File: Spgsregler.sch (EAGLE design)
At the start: 13 parts, among them X4 22-23-2031, X5 22-23-2031

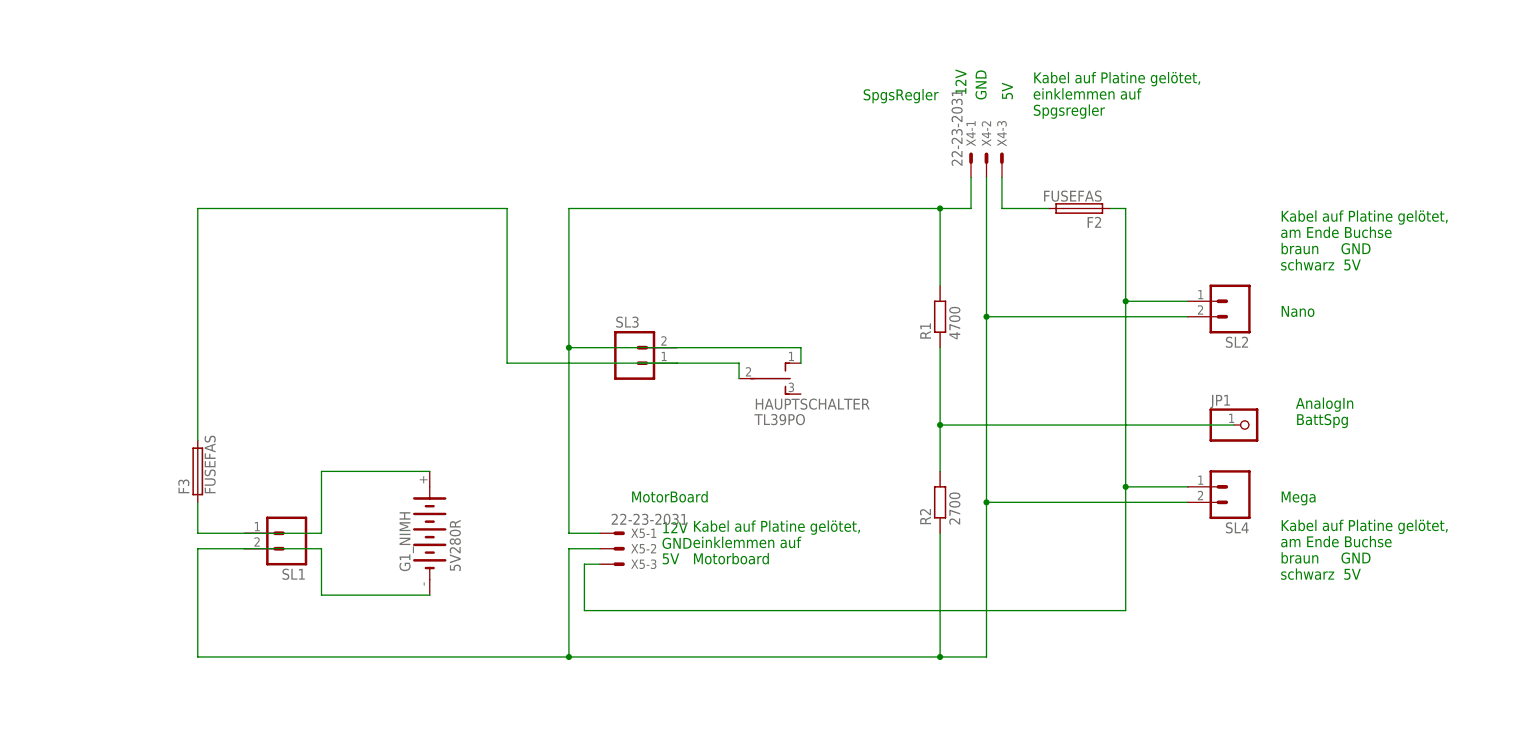
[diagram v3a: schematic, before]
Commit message: 
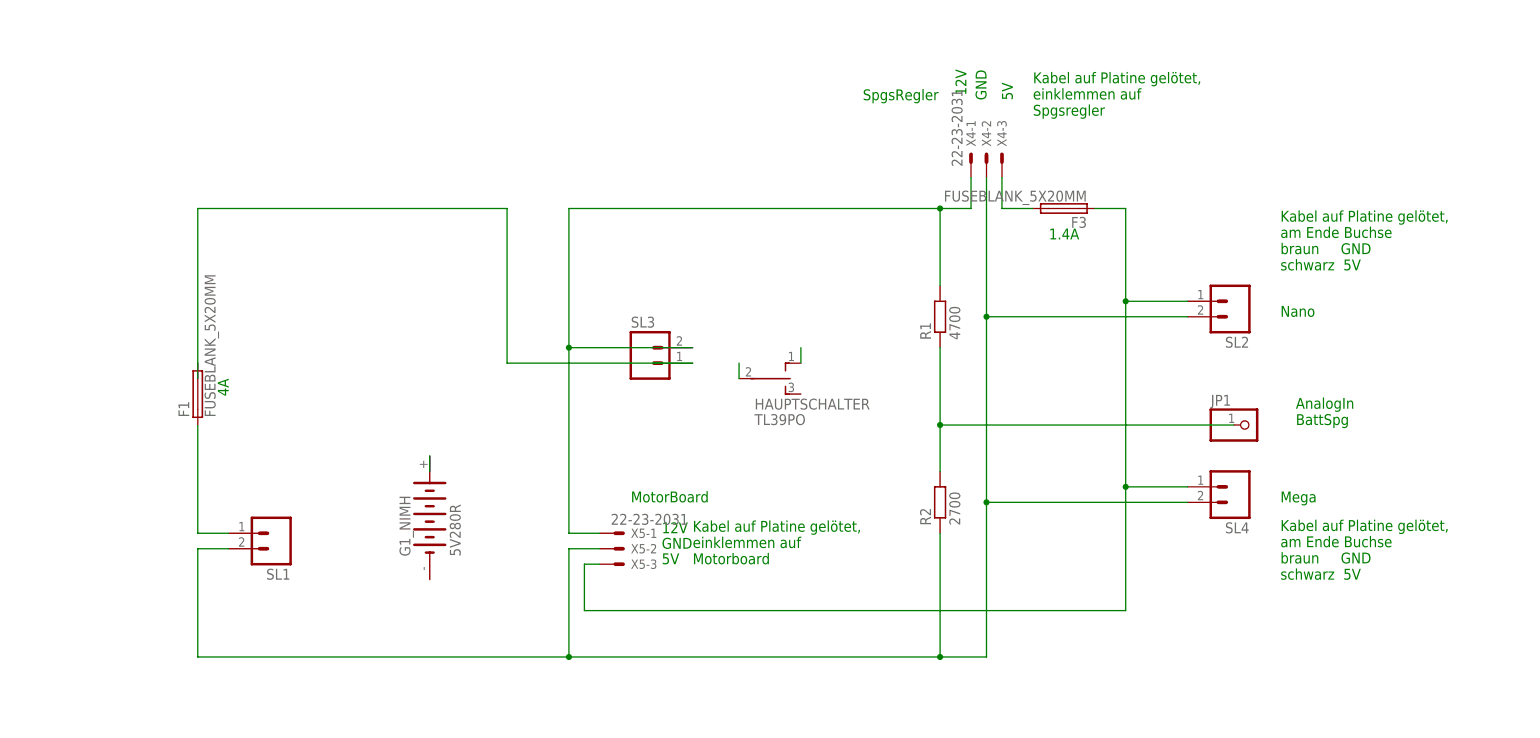
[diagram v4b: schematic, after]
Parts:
- removed F2: FUSEFAS, fuse:FUSEFAS
- added F1: FUSEBLANK_5X20MM, fuse:FUSEBLANK_5X20MM
- F3: value FUSEFAS -> FUSEBLANK_5X20MM; device fuse:FUSEFAS -> fuse:FUSEBLANK_5X20MM
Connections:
- removed net N$12: F2.1, SL2.1, SL4.1, X5-3.S
- new net N$1: F3.2, X4-3.S
- new net N$10: HAUPTSCHALTER.P
- new net N$7: G1_NIMH.+, G1_NIMH.+@1
- new net N$9: HAUPTSCHALTER.O
- net N$2: no longer G1_NIMH.-
- net N$4: now also F1.1, SL1.1; no longer F3.1, G1_NIMH.+
- net N$5: now also SL3.2; no longer HAUPTSCHALTER.O
- net N$6: now also F3.1, SL2.1, SL4.1, X5-3.S; no longer F2.2, X4-3.S
- net N$8: now also F1.2; no longer F3.2, HAUPTSCHALTER.P
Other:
- note added: "1.4A"
- note added: "4A"
- moved on the sheet: F3, G1_NIMH, SL1, SL3
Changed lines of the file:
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@@
 <part name="HAUPTSCHALTER" library="switch" deviceset="TL39PO" device=""/>
 <part name="JP1" library="pinhead" deviceset="PINHD-1X1" device=""/>
-<part name="F2" library="fuse" deviceset="FUSE" device="FAS"/>
 <part name="X4" library="con-molex" deviceset="22-23-2031" device=""/>
 <part name="X5" library="con-molex" deviceset="22-23-2031" device=""/>
@@
 <part name="SL2" library="con-amp-quick" deviceset="M02" device=""/>
 <part name="SL4" library="con-amp-quick" deviceset="M02" device=""/>
-<part name="F3" library="fuse" deviceset="FUSE" device="FAS"/>
 <part name="R1" library="rcl" deviceset="R-EU_" device="0207/10" value="4700"/>
 <part name="R2" library="rcl" deviceset="R-EU_" device="0207/10" value="2700"/>
+<part name="F1" library="fuse" deviceset="FUSE" device="BLANK_5X20MM"/>
+<part name="F3" library="fuse" deviceset="FUSE" device="BLANK_5X20MM"/>
 </parts>
 <sheets>
@@
 einklemmen auf
 Spgsregler</text>
+<text x="149.86" y="73.66" size="1.778" layer="91" rot="MR0">1.4A</text>
+<text x="10.16" y="50.8" size="1.778" layer="91" rot="MR270">4A</text>
 </plain>
 <instances>
-<instance part="G1_NIMH" gate="G$1" x="43.18" y="25.4" rot="R90"/>
-<instance part="SL1" gate="G$1" x="20.32" y="25.4" rot="R180"/>
-<instance part="SL3" gate="G$1" x="76.2" y="53.34"/>
+<instance part="G1_NIMH" gate="G$1" x="43.18" y="27.94" rot="R90"/>
+<instance part="SL1" gate="G$1" x="17.78" y="25.4" rot="R180"/>
+<instance part="SL3" gate="G$1" x="78.74" y="53.34"/>
 <instance part="HAUPTSCHALTER" gate="BEF1" x="99.06" y="50.8" rot="R270"/>
 <instance part="JP1" gate="G$1" x="177.8" y="43.18"/>
-<instance part="F2" gate="G$1" x="149.86" y="78.74" rot="R180"/>
 <instance part="X4" gate="-1" x="132.08" y="86.36" rot="R90"/>
 <instance part="X4" gate="-2" x="134.62" y="86.36" rot="R90"/>
@@
 <instance part="SL2" gate="G$1" x="175.26" y="63.5" rot="R180"/>
 <instance part="SL4" gate="G$1" x="175.26" y="33.02" rot="R180"/>
-<instance part="F3" gate="G$1" x="5.08" y="35.56" rot="R90"/>
 <instance part="R1" gate="G$1" x="127" y="60.96" rot="R90"/>
 <instance part="R2" gate="G$1" x="127" y="30.48" rot="R90"/>
+<instance part="F1" gate="G$1" x="5.08" y="48.26" rot="R90"/>
+<instance part="F3" gate="G$1" x="147.32" y="78.74" rot="R180"/>
 </instances>
 <busses>
@@
 <net name="N$8" class="0">
 <segment>
-<pinref part="F3" gate="G$1" pin="2"/>
-<wire x1="83.82" y1="53.34" x2="55.88" y2="53.34" width="0.1524" layer="91"/>
+<wire x1="86.36" y1="53.34" x2="55.88" y2="53.34" width="0.1524" layer="91"/>
 <wire x1="55.88" y1="78.74" x2="55.88" y2="53.34" width="0.1524" layer="91"/>
 <wire x1="5.08" y1="78.74" x2="55.88" y2="78.74" width="0.1524" layer="91"/>
-<wire x1="5.08" y1="40.64" x2="5.08" y2="78.74" width="0.1524" layer="91"/>
 <pinref part="SL3" gate="G$1" pin="1"/>
-<pinref part="HAUPTSCHALTER" gate="BEF1" pin="P"/>
-<wire x1="83.82" y1="53.34" x2="93.98" y2="53.34" width="0.1524" layer="91"/>
-<wire x1="93.98" y1="53.34" x2="93.98" y2="50.8" width="0.1524" layer="91"/>
-</segment>
-</net>
-<net name="N$12" class="0">
-<segment>
-<wire x1="157.48" y1="78.74" x2="157.48" y2="63.5" width="0.1524" layer="91"/>
-<wire x1="157.48" y1="63.5" x2="157.48" y2="33.02" width="0.1524" layer="91"/>
-<wire x1="157.48" y1="33.02" x2="157.48" y2="12.7" width="0.1524" layer="91"/>
-<wire x1="157.48" y1="12.7" x2="68.58" y2="12.7" width="0.1524" layer="91"/>
-<wire x1="68.58" y1="12.7" x2="68.58" y2="20.32" width="0.1524" layer="91"/>
-<pinref part="F2" gate="G$1" pin="1"/>
-<wire x1="154.94" y1="78.74" x2="157.48" y2="78.74" width="0.1524" layer="91"/>
-<pinref part="SL2" gate="G$1" pin="1"/>
-<wire x1="167.64" y1="63.5" x2="157.48" y2="63.5" width="0.1524" layer="91"/>
-<junction x="157.48" y="63.5"/>
-<pinref part="SL4" gate="G$1" pin="1"/>
-<wire x1="167.64" y1="33.02" x2="157.48" y2="33.02" width="0.1524" layer="91"/>
-<junction x="157.48" y="33.02"/>
-<pinref part="X5" gate="-3" pin="S"/>
-<wire x1="68.58" y1="20.32" x2="71.12" y2="20.32" width="0.1524" layer="91"/>
-</segment>
-</net>
-<net name="N$4" class="0">
-<segment>
-<pinref part="G1_NIMH" gate="G$1" pin="+"/>
-<wire x1="43.18" y1="35.56" x2="25.4" y2="35.56" width="0.1524" layer="91"/>
-<wire x1="25.4" y1="35.56" x2="25.4" y2="25.4" width="0.1524" layer="91"/>
-<pinref part="F3" gate="G$1" pin="1"/>
-<wire x1="5.08" y1="30.48" x2="5.08" y2="25.4" width="0.1524" layer="91"/>
-<wire x1="25.4" y1="25.4" x2="5.08" y2="25.4" width="0.1524" layer="91"/>
+<pinref part="F1" gate="G$1" pin="2"/>
+<wire x1="5.08" y1="50.8" x2="5.08" y2="53.34" width="0.1524" layer="91"/>
+<wire x1="5.08" y1="78.74" x2="5.08" y2="53.34" width="0.1524" layer="91"/>
 </segment>
 </net>
 <net name="N$5" class="0">
 <segment>
-<wire x1="66.04" y1="55.88" x2="66.04" y2="78.74" width="0.1524" layer="91"/>
 <wire x1="66.04" y1="78.74" x2="127" y2="78.74" width="0.1524" layer="91"/>
 <wire x1="127" y1="78.74" x2="132.08" y2="78.74" width="0.1524" layer="91"/>
+<wire x1="66.04" y1="78.74" x2="66.04" y2="55.88" width="0.1524" layer="91"/>
 <wire x1="66.04" y1="55.88" x2="66.04" y2="25.4" width="0.1524" layer="91"/>
 <wire x1="66.04" y1="25.4" x2="71.12" y2="25.4" width="0.1524" layer="91"/>
-<junction x="66.04" y="55.88"/>
 <pinref part="X5" gate="-1" pin="S"/>
 <pinref part="X4" gate="-1" pin="S"/>
 <wire x1="132.08" y1="78.74" x2="132.08" y2="83.82" width="0.1524" layer="91"/>
-<pinref part="HAUPTSCHALTER" gate="BEF1" pin="O"/>
-<wire x1="104.14" y1="53.34" x2="104.14" y2="55.88" width="0.1524" layer="91"/>
-<wire x1="104.14" y1="55.88" x2="66.04" y2="55.88" width="0.1524" layer="91"/>
 <pinref part="R1" gate="G$1" pin="2"/>
 <wire x1="127" y1="66.04" x2="127" y2="78.74" width="0.1524" layer="91"/>
 <junction x="127" y="78.74"/>
+<pinref part="SL3" gate="G$1" pin="2"/>
+<wire x1="66.04" y1="55.88" x2="86.36" y2="55.88" width="0.1524" layer="91"/>
+<junction x="66.04" y="55.88"/>
 </segment>
 </net>
@@
 <net name="N$6" class="0">
 <segment>
-<pinref part="F2" gate="G$1" pin="2"/>
-<wire x1="137.16" y1="78.74" x2="144.78" y2="78.74" width="0.1524" layer="91"/>
-<pinref part="X4" gate="-3" pin="S"/>
-<wire x1="137.16" y1="78.74" x2="137.16" y2="83.82" width="0.1524" layer="91"/>
+<wire x1="157.48" y1="78.74" x2="157.48" y2="63.5" width="0.1524" layer="91"/>
+<wire x1="157.48" y1="63.5" x2="157.48" y2="33.02" width="0.1524" layer="91"/>
+<wire x1="157.48" y1="33.02" x2="157.48" y2="12.7" width="0.1524" layer="91"/>
+<wire x1="157.48" y1="12.7" x2="68.58" y2="12.7" width="0.1524" layer="91"/>
+<wire x1="68.58" y1="12.7" x2="68.58" y2="20.32" width="0.1524" layer="91"/>
+<pinref part="SL2" gate="G$1" pin="1"/>
+<wire x1="167.64" y1="63.5" x2="157.48" y2="63.5" width="0.1524" layer="91"/>
+<junction x="157.48" y="63.5"/>
+<pinref part="SL4" gate="G$1" pin="1"/>
+<wire x1="167.64" y1="33.02" x2="157.48" y2="33.02" width="0.1524" layer="91"/>
+<junction x="157.48" y="33.02"/>
+<pinref part="X5" gate="-3" pin="S"/>
+<wire x1="68.58" y1="20.32" x2="71.12" y2="20.32" width="0.1524" layer="91"/>
+<pinref part="F3" gate="G$1" pin="1"/>
+<wire x1="157.48" y1="78.74" x2="152.4" y2="78.74" width="0.1524" layer="91"/>
 </segment>
 </net>
 <net name="N$2" class="0">
 <segment>
-<pinref part="G1_NIMH" gate="G$1" pin="-"/>
-<wire x1="25.4" y1="15.24" x2="43.18" y2="15.24" width="0.1524" layer="91"/>
-<wire x1="25.4" y1="15.24" x2="25.4" y2="22.86" width="0.1524" layer="91"/>
 <pinref part="SL1" gate="G$1" pin="2"/>
-<wire x1="12.7" y1="22.86" x2="5.08" y2="22.86" width="0.1524" layer="91"/>
+<wire x1="10.16" y1="22.86" x2="5.08" y2="22.86" width="0.1524" layer="91"/>
 <wire x1="5.08" y1="5.08" x2="66.04" y2="5.08" width="0.1524" layer="91"/>
 <wire x1="71.12" y1="22.86" x2="66.04" y2="22.86" width="0.1524" layer="91"/>
@@
 <wire x1="127" y1="25.4" x2="127" y2="5.08" width="0.1524" layer="91"/>
 <junction x="127" y="5.08"/>
-<wire x1="25.4" y1="22.86" x2="12.7" y2="22.86" width="0.1524" layer="91"/>
 </segment>
 </net>
+<net name="N$1" class="0">
+<segment>
+<pinref part="X4" gate="-3" pin="S"/>
+<pinref part="F3" gate="G$1" pin="2"/>
+<wire x1="137.16" y1="78.74" x2="142.24" y2="78.74" width="0.1524" layer="91"/>
+<wire x1="137.16" y1="78.74" x2="137.16" y2="83.82" width="0.1524" layer="91"/>
+</segment>
+</net>
+<net name="N$4" class="0">
+<segment>
+<pinref part="SL1" gate="G$1" pin="1"/>
+<wire x1="10.16" y1="25.4" x2="5.08" y2="25.4" width="0.1524" layer="91"/>
+<pinref part="F1" gate="G$1" pin="1"/>
+<wire x1="5.08" y1="25.4" x2="5.08" y2="43.18" width="0.1524" layer="91"/>
+</segment>
+</net>
+<net name="N$7" class="0">
+<segment>
+<pinref part="G1_NIMH" gate="G$1" pin="+"/>
+<pinref part="G1_NIMH" gate="G$1" pin="+@1"/>
+<wire x1="43.18" y1="35.56" x2="43.18" y2="38.1" width="0.1524" layer="91"/>
+</segment>
+</net>
+<net name="N$9" class="0">
+<segment>
+<pinref part="HAUPTSCHALTER" gate="BEF1" pin="O"/>
+<wire x1="104.14" y1="53.34" x2="104.14" y2="55.88" width="0.1524" layer="91"/>
+</segment>
+</net>
+<net name="N$10" class="0">
+<segment>
+<pinref part="HAUPTSCHALTER" gate="BEF1" pin="P"/>
+<wire x1="93.98" y1="53.34" x2="93.98" y2="50.8" width="0.1524" layer="91"/>
+</segment>
+</net>

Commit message: 
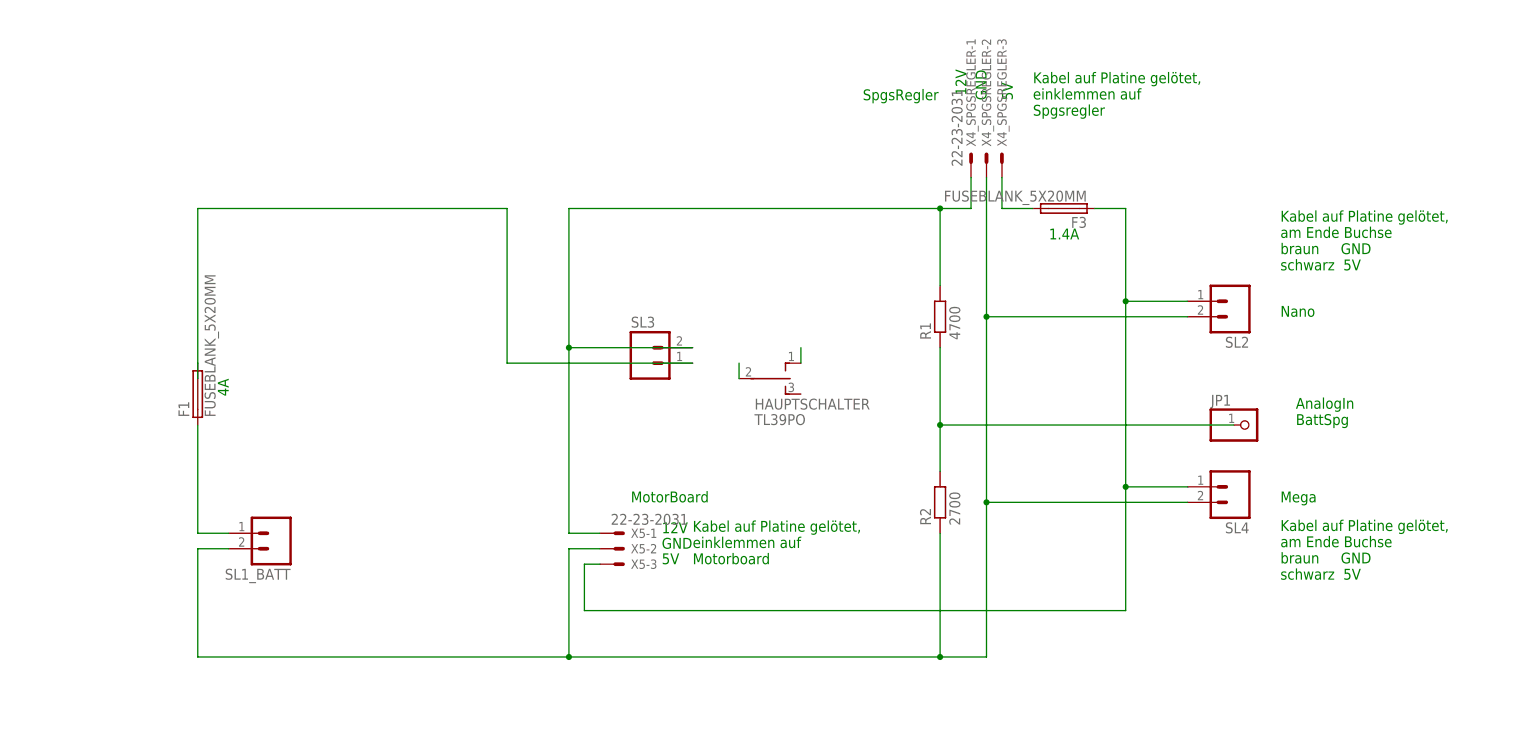
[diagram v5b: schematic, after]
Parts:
- removed G1_NIMH: 5V280R, battery:5V280R
- renumbered SL1 to SL1_BATT, X4 to X4_SPGSREGLER
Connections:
- removed net N$7: G1_NIMH.+, G1_NIMH.+@1
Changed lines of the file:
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@@
 <?xml version="1.0" encoding="utf-8"?>
 <!DOCTYPE eagle SYSTEM "eagle.dtd">
-<eagle version="7.7.0">
+<eagle version="8.5.1">
 <drawing>
 <settings>
 <setting alwaysvectorfont="no"/>
+<setting keepoldvectorfont="yes"/>
 <setting verticaltext="up"/>
 </settings>
@@
 </classes>
 <parts>
-<part name="G1_NIMH" library="battery" deviceset="5V280R" device=""/>
-<part name="SL1" library="con-amp-quick" deviceset="M02" device=""/>
+<part name="SL1_BATT" library="con-amp-quick" deviceset="M02" device=""/>
 <part name="SL3" library="con-amp-quick" deviceset="M02" device=""/>
 <part name="HAUPTSCHALTER" library="switch" deviceset="TL39PO" device=""/>
 <part name="JP1" library="pinhead" deviceset="PINHD-1X1" device=""/>
-<part name="X4" library="con-molex" deviceset="22-23-2031" device=""/>
+<part name="X4_SPGSREGLER" library="con-molex" deviceset="22-23-2031" device=""/>
 <part name="X5" library="con-molex" deviceset="22-23-2031" device=""/>
 <part name="FRAME1" library="frames" deviceset="A4L-LOC" device="" value="WERTWERT"/>
@@
 </plain>
 <instances>
-<instance part="G1_NIMH" gate="G$1" x="43.18" y="27.94" rot="R90"/>
-<instance part="SL1" gate="G$1" x="17.78" y="25.4" rot="R180"/>
+<instance part="SL1_BATT" gate="G$1" x="17.78" y="25.4" rot="R180"/>
 <instance part="SL3" gate="G$1" x="78.74" y="53.34"/>
 <instance part="HAUPTSCHALTER" gate="BEF1" x="99.06" y="50.8" rot="R270"/>
 <instance part="JP1" gate="G$1" x="177.8" y="43.18"/>
-<instance part="X4" gate="-1" x="132.08" y="86.36" rot="R90"/>
-<instance part="X4" gate="-2" x="134.62" y="86.36" rot="R90"/>
-<instance part="X4" gate="-3" x="137.16" y="86.36" rot="R90"/>
+<instance part="X4_SPGSREGLER" gate="-1" x="132.08" y="86.36" rot="R90"/>
+<instance part="X4_SPGSREGLER" gate="-2" x="134.62" y="86.36" rot="R90"/>
+<instance part="X4_SPGSREGLER" gate="-3" x="137.16" y="86.36" rot="R90"/>
 <instance part="X5" gate="-1" x="73.66" y="25.4"/>
 <instance part="X5" gate="-2" x="73.66" y="22.86"/>
@@
 <wire x1="66.04" y1="25.4" x2="71.12" y2="25.4" width="0.1524" layer="91"/>
 <pinref part="X5" gate="-1" pin="S"/>
-<pinref part="X4" gate="-1" pin="S"/>
+<pinref part="X4_SPGSREGLER" gate="-1" pin="S"/>
 <wire x1="132.08" y1="78.74" x2="132.08" y2="83.82" width="0.1524" layer="91"/>
 <pinref part="R1" gate="G$1" pin="2"/>
@@
 <net name="N$2" class="0">
 <segment>
-<pinref part="SL1" gate="G$1" pin="2"/>
+<pinref part="SL1_BATT" gate="G$1" pin="2"/>
 <wire x1="10.16" y1="22.86" x2="5.08" y2="22.86" width="0.1524" layer="91"/>
 <wire x1="5.08" y1="5.08" x2="66.04" y2="5.08" width="0.1524" layer="91"/>
@@
 <wire x1="134.62" y1="60.96" x2="134.62" y2="30.48" width="0.1524" layer="91"/>
 <wire x1="134.62" y1="30.48" x2="134.62" y2="5.08" width="0.1524" layer="91"/>
-<pinref part="X4" gate="-2" pin="S"/>
+<pinref part="X4_SPGSREGLER" gate="-2" pin="S"/>
 <pinref part="SL2" gate="G$1" pin="2"/>
 <wire x1="167.64" y1="60.96" x2="134.62" y2="60.96" width="0.1524" layer="91"/>
@@
 <net name="N$1" class="0">
 <segment>
-<pinref part="X4" gate="-3" pin="S"/>
+<pinref part="X4_SPGSREGLER" gate="-3" pin="S"/>
 <pinref part="F3" gate="G$1" pin="2"/>
 <wire x1="137.16" y1="78.74" x2="142.24" y2="78.74" width="0.1524" layer="91"/>
@@
 <net name="N$4" class="0">
 <segment>
-<pinref part="SL1" gate="G$1" pin="1"/>
+<pinref part="SL1_BATT" gate="G$1" pin="1"/>
 <wire x1="10.16" y1="25.4" x2="5.08" y2="25.4" width="0.1524" layer="91"/>
 <pinref part="F1" gate="G$1" pin="1"/>
@@
 </segment>
 </net>
-<net name="N$7" class="0">
-<segment>
-<pinref part="G1_NIMH" gate="G$1" pin="+"/>
-<pinref part="G1_NIMH" gate="G$1" pin="+@1"/>
-<wire x1="43.18" y1="35.56" x2="43.18" y2="38.1" width="0.1524" layer="91"/>
-</segment>
-</net>
